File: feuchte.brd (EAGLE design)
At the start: 100 x 80 mm, 17 parts, among them IC1 ULN2003AD, IC2 IP4234CZ6, K1 G5LA, Q1 12MHz, U1 ATMEGA32U2-AU

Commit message: Bibliothek hinzugefügt
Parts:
- C1, C4, C5, C6, C7, R1, R2, R3: device eigene:0603 -> Bauelemente:0603
- C2, C3: device resistor:C0603K -> Bauelemente:0603
- IC2: value IP4234CZ6 -> ESD_USB_IP4234CZ6; device eigene:USB-ESD-IP4234CZ6 -> Bauelemente:USB_ESD_IP4234CZ6
- K1: value G5LA -> RELAY_G5LA; device eigene:G5LA -> Bauelemente:RELAY_G5LA
- Q1: device eigene:QUARZ-ABMM2 -> Bauelemente:QUARTZ_ABMM2
- U$1: value CON-SPI-10 -> CON_SPI_AVR10; device eigene:AVR-ISP-10 -> Bauelemente:CON_ISP_AVR10
- U1: value ATMEGA32U2-AU -> MCU_ATMEGA32U2-AU; device eigene:QFP80P900X900X120-32N -> Bauelemente:TQFP32-0.8
- USB1: value CON-MICROUSB-ZX62R-B-5P -> CON_MICROUSB_ZX62R-B-5P; device eigene:CON-MICROUSB_ZX62R-B-5P -> Bauelemente:CON_MICROUSB_ZX62R-B-5P
- moved C7 71.9 mm to (11.4, 37.9)
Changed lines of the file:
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@@
 </autorouter>
 <elements>
-<element name="U1" library="eigene" package="QFP80P900X900X120-32N" value="ATMEGA32U2-AU" x="40" y="20" rot="R90">
+<element name="U1" library="Bauelemente" package="TQFP32-0.8" value="MCU_ATMEGA32U2-AU" x="40" y="20" rot="R90">
 <attribute name="PACKAGE" value="TQFP-32" x="48.89" y="45.4" size="1.778" layer="27" rot="R90" display="off"/>
 <attribute name="OC_NEWARK" value="26R5632" x="48.89" y="45.4" size="1.778" layer="27" rot="R90" display="off"/>
@@
 <attribute name="OC_FARNELL" value="1748524" x="48.89" y="45.4" size="1.778" layer="27" rot="R90" display="off"/>
 </element>
-<element name="K1" library="eigene" package="G5LA" value="G5LA" x="-34.29" y="26.67"/>
+<element name="K1" library="Bauelemente" package="RELAY_G5LA" value="RELAY_G5LA" x="-34.29" y="26.67"/>
 <element name="IC1" library="uln-udn" package="SO16" value="ULN2003AD" x="-20.32" y="48.26"/>
-<element name="R1" library="eigene" package="0603" value="1k" x="-30.48" y="46.99"/>
-<element name="C1" library="eigene" package="0603" value="100n" x="9" y="17" rot="R270"/>
-<element name="Q1" library="eigene" package="QUARZ-ABMM2" value="12MHz" x="36" y="9"/>
-<element name="C2" library="resistor" package="C0603K" value="33p" x="36" y="5"/>
-<element name="C3" library="resistor" package="C0603K" value="33p" x="42" y="9" rot="R270"/>
-<element name="C4" library="eigene" package="0603" value="100n" x="30" y="16" rot="R270"/>
-<element name="C5" library="eigene" package="0603" value="1µ" x="30" y="21.55"/>
-<element name="C6" library="eigene" package="0603" value="10µ" x="21" y="16" rot="R270"/>
-<element name="R2" library="eigene" package="0603" value="22" x="25" y="19.95"/>
-<element name="R3" library="eigene" package="0603" value="22" x="25" y="18.45"/>
-<element name="USB1" library="eigene" package="CON-MICROUSB_ZX62R-B-5P" value="CON-MICROUSB-ZX62R-B-5P" x="4.8" y="19.525" rot="R270"/>
-<element name="IC2" library="eigene" package="USB-ESD-IP4234CZ6" value="IP4234CZ6" x="15" y="19.2" rot="R180"/>
-<element name="U$1" library="eigene" package="AVR-ISP-10" value="CON-SPI-10" x="43.4" y="29.8" rot="R180"/>
-<element name="C7" library="eigene" package="0603" value="100n" x="-37.9" y="-14.4"/>
+<element name="R1" library="Bauelemente" package="0603" value="1k" x="-30.48" y="46.99"/>
+<element name="C1" library="Bauelemente" package="0603" value="100n" x="9" y="17" rot="R270"/>
+<element name="Q1" library="Bauelemente" package="QUARTZ_ABMM2" value="12MHz" x="36" y="9"/>
+<element name="C2" library="Bauelemente" package="0603" value="33p" x="36" y="5"/>
+<element name="C3" library="Bauelemente" package="0603" value="33p" x="42" y="9" rot="R270"/>
+<element name="C4" library="Bauelemente" package="0603" value="100n" x="30" y="16" rot="R270"/>
+<element name="C5" library="Bauelemente" package="0603" value="1µ" x="30" y="21.55"/>
+<element name="C6" library="Bauelemente" package="0603" value="10µ" x="21" y="16" rot="R270"/>
+<element name="R2" library="Bauelemente" package="0603" value="22" x="25" y="19.95"/>
+<element name="R3" library="Bauelemente" package="0603" value="22" x="25" y="18.45"/>
+<element name="USB1" library="Bauelemente" package="CON_MICROUSB_ZX62R-B-5P" value="CON_MICROUSB_ZX62R-B-5P" x="4.8" y="19.525" rot="R270"/>
+<element name="IC2" library="Bauelemente" package="USB_ESD_IP4234CZ6" value="ESD_USB_IP4234CZ6" x="15" y="19.2" rot="R180"/>
+<element name="U$1" library="Bauelemente" package="CON_ISP_AVR10" value="CON_SPI_AVR10" x="43.4" y="29.8" rot="R180"/>
+<element name="C7" library="Bauelemente" package="0603" value="100n" x="11.4" y="37.9"/>
 </elements>
 <signals>
@@
 <contactref element="Q1" pad="4"/>
 <contactref element="Q1" pad="2"/>
-<wire x1="36.875" y1="5" x2="37.9" y2="5" width="0.5" layer="1"/>
+<wire x1="36.85" y1="5" x2="37.9" y2="5" width="0.5" layer="1"/>
 <wire x1="37.9" y1="5" x2="38.2" y2="5.3" width="0.5" layer="1" curve="90"/>
 <wire x1="38.2" y1="5.3" x2="38.2" y2="7.8" width="0.5" layer="1"/>
-<wire x1="42" y1="8.125" x2="38.5" y2="8.125" width="0.5" layer="1"/>
+<wire x1="42" y1="8.15" x2="38.5" y2="8.125" width="0.5" layer="1"/>
 <wire x1="38.5" y1="8.125" x2="38.2" y2="7.825" width="0.5" layer="1" curve="90"/>
 <wire x1="38.2" y1="7.825" x2="38.2" y2="7.8" width="0.5" layer="1"/>
@@
 <contactref element="C2" pad="1"/>
 <contactref element="U1" pad="1"/>
-<wire x1="35.125" y1="5" x2="34.1" y2="5" width="0.5" layer="1"/>
+<wire x1="35.15" y1="5" x2="34.1" y2="5" width="0.5" layer="1"/>
 <wire x1="34.1" y1="5" x2="33.8" y2="5.3" width="0.5" layer="1" curve="-90"/>
 <wire x1="33.8" y1="5.3" x2="33.8" y2="7.8" width="0.5" layer="1"/>
@@
 <contactref element="C3" pad="1"/>
 <contactref element="U1" pad="2"/>
-<wire x1="42" y1="9.875" x2="38.5" y2="9.875" width="0.5" layer="1"/>
+<wire x1="42" y1="9.85" x2="38.5" y2="9.875" width="0.5" layer="1"/>
 <wire x1="38.5" y1="9.875" x2="38.2" y2="10.175" width="0.5" layer="1" curve="-90"/>
 <wire x1="38.2" y1="10.175" x2="38.2" y2="10.2" width="0.5" layer="1"/>

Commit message: SMD Bauteile auf Rückseite gespiegelt
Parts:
- moved R1 126.1 mm to (95.2, 57.3), flipped to the bottom
- moved IC1 113.2 mm to (91.7, 64.4), flipped to the bottom
- moved USB1 90.4 mm to (95.2, 19.5), flipped to the bottom
- moved C1 82.0 mm to (91.0, 17.0), flipped to the bottom
- moved C7 81.0 mm to (90.4, 56.0), flipped to the bottom
- moved IC2 70.0 mm to (85.0, 19.2), flipped to the bottom
- moved C6 58.0 mm to (79.0, 16.0), flipped to the bottom
- moved U$1 55.9 mm to (77.8, 73.8)
- moved R2 50.0 mm to (75.0, 19.9), flipped to the bottom
- moved R3 50.0 mm to (75.0, 18.4), flipped to the bottom
- moved C4 40.0 mm to (70.0, 16.0), flipped to the bottom
- moved C5 40.0 mm to (70.0, 21.6), flipped to the bottom
- moved C2 28.0 mm to (64.0, 5.00), flipped to the bottom
- moved Q1 28.0 mm to (64.0, 9.00), flipped to the bottom
- moved U1 20.0 mm to (60.0, 20.0), flipped to the bottom
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
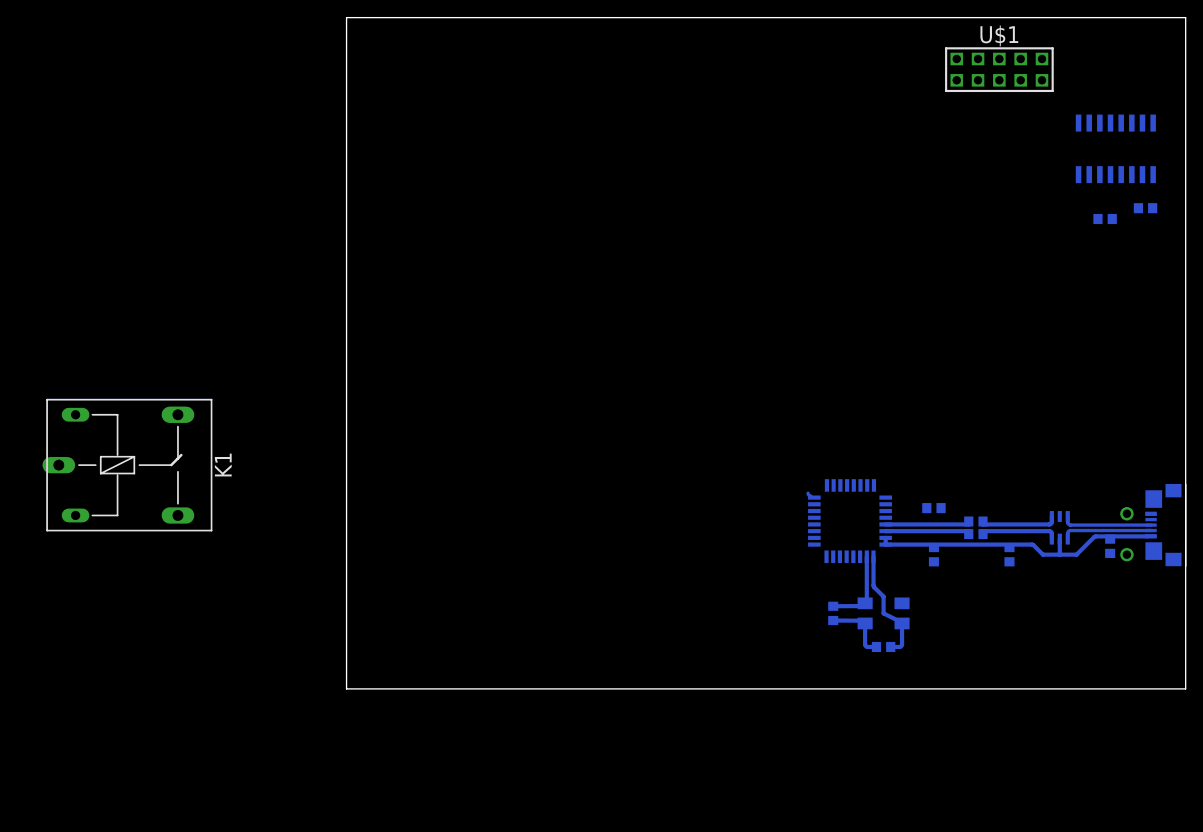
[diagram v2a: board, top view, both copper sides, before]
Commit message: ULN2003 aus Eagle verändert um fehler vom DRC zu entfernen und besser dem Datenblatt zu entsprechen
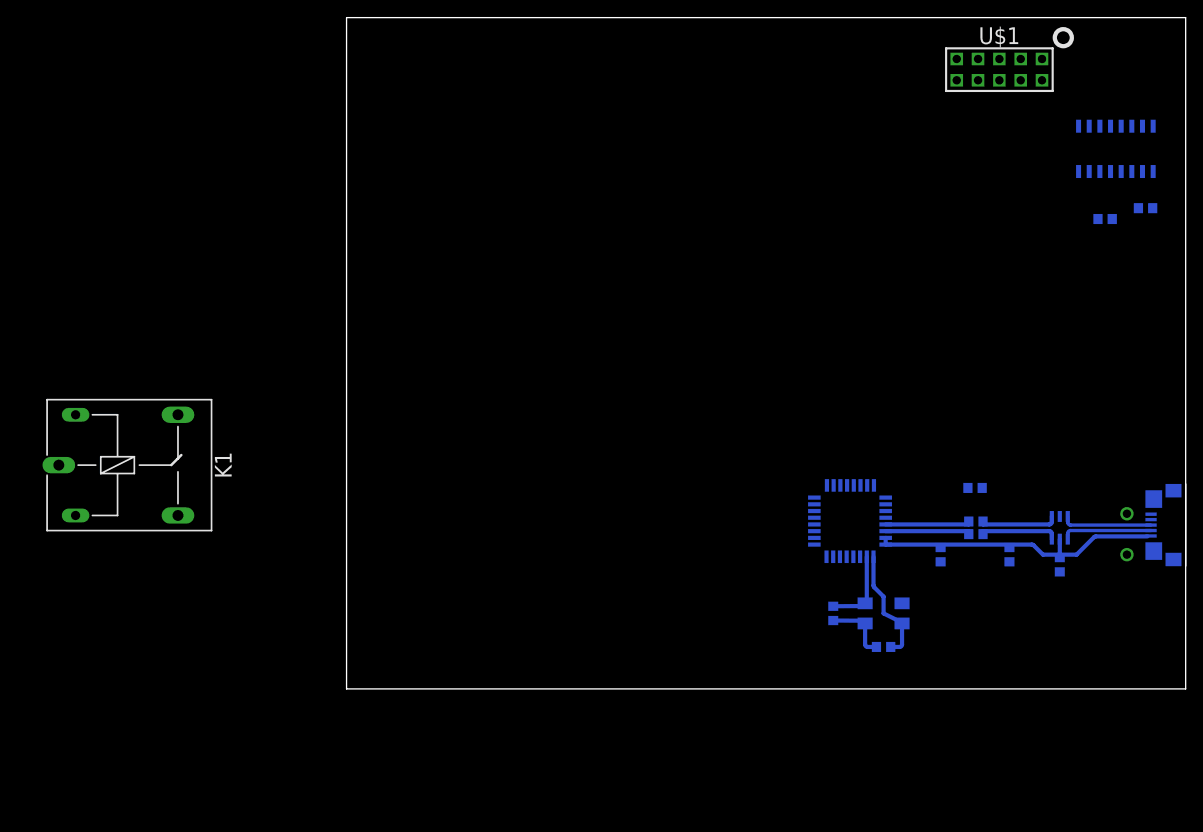
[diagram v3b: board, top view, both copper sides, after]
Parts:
- IC1: value ULN2003AD -> IC_ULN2003AD; device uln-udn:SO16 -> Bauelemente:SOIC16
- moved C1 6.39 mm to (85.0, 14.8)
- moved C5 5.46 mm to (74.9, 23.9)
- moved C4 0.80 mm to (70.8, 16.0)
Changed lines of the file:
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@@
 <layer number="24" name="bOrigins" color="15" fill="1" visible="yes" active="yes"/>
 <layer number="25" name="tNames" color="7" fill="1" visible="yes" active="yes"/>
-<layer number="26" name="bNames" color="7" fill="1" visible="yes" active="yes"/>
+<layer number="26" name="bNames" color="7" fill="1" visible="no" active="yes"/>
 <layer number="27" name="tValues" color="7" fill="1" visible="yes" active="yes"/>
-<layer number="28" name="bValues" color="7" fill="1" visible="yes" active="yes"/>
+<layer number="28" name="bValues" color="7" fill="1" visible="no" active="yes"/>
 <layer number="29" name="tStop" color="7" fill="3" visible="yes" active="yes"/>
 <layer number="30" name="bStop" color="7" fill="6" visible="yes" active="yes"/>
@@
 <wire x1="100" y1="80" x2="0" y2="80" width="0" layer="20"/>
 <wire x1="0" y1="80" x2="0" y2="0" width="0" layer="20"/>
-<rectangle x1="95.2" y1="17.925" x2="96.55" y2="18.425" layer="16" rot="R180"/>
-<rectangle x1="95.2" y1="20.625" x2="96.55" y2="21.125" layer="16" rot="R180"/>
 </plain>
 <attributes>
@@
 </element>
 <element name="K1" library="Bauelemente" package="RELAY_G5LA" value="RELAY_G5LA" x="-34.29" y="26.67"/>
-<element name="IC1" library="uln-udn" package="SO16" value="ULN2003AD" x="91.68" y="64.36" rot="MR0"/>
+<element name="IC1" library="Bauelemente" package="SOIC16" value="IC_ULN2003AD" x="91.68" y="64.36" rot="MR0"/>
 <element name="R1" library="Bauelemente" package="0603" value="1k" x="95.22" y="57.29" rot="MR0"/>
-<element name="C1" library="Bauelemente" package="0603" value="100n" x="91" y="17" rot="MR270"/>
+<element name="C1" library="Bauelemente" package="0603" value="100n" x="85" y="14.8" rot="MR270"/>
 <element name="Q1" library="Bauelemente" package="QUARTZ_ABMM2" value="12MHz" x="64" y="9" rot="MR0"/>
 <element name="C2" library="Bauelemente" package="0603" value="33p" x="64" y="5" rot="MR0"/>
 <element name="C3" library="Bauelemente" package="0603" value="33p" x="58" y="9" rot="MR270"/>
-<element name="C4" library="Bauelemente" package="0603" value="100n" x="70" y="16" rot="MR270"/>
-<element name="C5" library="Bauelemente" package="0603" value="1µ" x="70" y="21.55" rot="MR0"/>
+<element name="C4" library="Bauelemente" package="0603" value="100n" x="70.8" y="16" rot="MR270"/>
+<element name="C5" library="Bauelemente" package="0603" value="1µ" x="74.9" y="23.95" rot="MR0"/>
 <element name="C6" library="Bauelemente" package="0603" value="10µ" x="79" y="16" rot="MR270"/>
 <element name="R2" library="Bauelemente" package="0603" value="22" x="75" y="19.95" rot="MR0"/>
@@
 <signals>
 <signal name="GND" airwireshidden="yes">
-<contactref element="IC1" pad="8"/>
 <contactref element="USB1" pad="5"/>
 <contactref element="IC2" pad="2"/>
@@
 <contactref element="U$1" pad="6"/>
 <contactref element="U$1" pad="4"/>
+<contactref element="IC1" pad="8"/>
 <wire x1="77.8" y1="72.53" x2="80.34" y2="72.53" width="0" layer="19" extent="1-1"/>
 <wire x1="75.26" y1="72.53" x2="77.8" y2="72.53" width="0" layer="19" extent="1-1"/>
 <wire x1="72.72" y1="72.53" x2="75.26" y2="72.53" width="0" layer="19" extent="1-1"/>
-<wire x1="55.75" y1="20.4" x2="77.8" y2="72.53" width="0" layer="19" extent="1-1"/>
-<wire x1="61.2" y1="15.75" x2="55.75" y2="20.4" width="0" layer="19" extent="1-1"/>
-<wire x1="64.25" y1="20.4" x2="61.2" y2="15.75" width="0" layer="19" extent="1-1"/>
-<wire x1="70.85" y1="21.55" x2="64.25" y2="20.4" width="0" layer="19" extent="1-1"/>
-<wire x1="70" y1="15.15" x2="70.85" y2="21.55" width="0" layer="19" extent="1-1"/>
-<wire x1="66.2" y1="10.2" x2="70" y2="15.15" width="0" layer="19" extent="1-1"/>
-<wire x1="61.8" y1="7.825" x2="66.2" y2="10.2" width="0" layer="19" extent="1-1"/>
-<wire x1="79" y1="15.15" x2="70" y2="15.15" width="0" layer="19" extent="1-1"/>
-<wire x1="85" y1="20.55" x2="79" y2="15.15" width="0" layer="19" extent="1-1"/>
-<wire x1="91" y1="16.15" x2="85" y2="20.55" width="0" layer="19" extent="1-1"/>
-<wire x1="93" y1="16" x2="91" y2="16.15" width="0" layer="19" extent="1-1"/>
-<wire x1="93" y1="20.875" x2="93" y2="16" width="0" layer="19" extent="1-1"/>
-<wire x1="95.875" y1="20.825" x2="93" y2="20.875" width="0" layer="19" extent="1-1"/>
-<wire x1="87.235" y1="61.2866" x2="95.875" y2="20.875" width="0" layer="19" extent="1-1"/>
+<wire x1="87.235" y1="61.66" x2="80.34" y2="72.53" width="0" layer="19" extent="16-16"/>
+<wire x1="75.75" y1="23.95" x2="87.235" y2="61.66" width="0" layer="19" extent="16-16"/>
+<wire x1="79" y1="15.15" x2="75.75" y2="23.95" width="0" layer="19" extent="16-16"/>
+<wire x1="85" y1="13.95" x2="79" y2="15.15" width="0" layer="19" extent="16-16"/>
+<wire x1="85" y1="20.55" x2="85" y2="13.95" width="0" layer="19" extent="16-16"/>
+<wire x1="93" y1="20.875" x2="85" y2="20.55" width="0" layer="19" extent="16-16"/>
+<wire x1="95.875" y1="20.825" x2="93" y2="20.875" width="0" layer="19" extent="16-16"/>
+<wire x1="93" y1="16" x2="93" y2="20.875" width="0" layer="19" extent="1-1"/>
+<wire x1="70.8" y1="15.15" x2="79" y2="15.15" width="0" layer="19" extent="16-16"/>
+<wire x1="66.2" y1="10.2" x2="70.8" y2="15.15" width="0" layer="19" extent="16-16"/>
+<wire x1="61.8" y1="7.8" x2="66.2" y2="10.2" width="0" layer="19" extent="16-16"/>
+<wire x1="61.2" y1="15.75" x2="66.2" y2="10.2" width="0" layer="19" extent="16-16"/>
+<wire x1="64.25" y1="20.4" x2="61.2" y2="15.75" width="0" layer="19" extent="16-16"/>
+<wire x1="55.75" y1="20.4" x2="61.2" y2="15.75" width="0" layer="19" extent="16-16"/>
 </signal>
 <signal name="N$1">
@@
 <wire x1="85.95" y1="18.55" x2="86.275" y2="18.875" width="0.4" layer="16" curve="-90"/>
 <wire x1="86.275" y1="18.875" x2="95.875" y2="18.875" width="0.4" layer="16"/>
-<wire x1="85.95" y1="18.225" x2="85.95" y2="17.85" width="0" layer="19" extent="1-1"/>
+<wire x1="85.95" y1="18.225" x2="85.95" y2="17.85" width="0" layer="19" extent="16-16"/>
 </signal>
 <signal name="USBCON_P">
@@
 <contactref element="C4" pad="1"/>
 <contactref element="U$1" pad="2"/>
-<wire x1="60.4" y1="15.75" x2="82.88" y2="72.53" width="0" layer="19" extent="1-1"/>
-<wire x1="64.25" y1="17.2" x2="60.4" y2="15.75" width="0" layer="19" extent="1-1"/>
-<wire x1="91" y1="17.85" x2="89.299265625" y2="18.175" width="0" layer="19" extent="1-1"/>
-<wire x1="79" y1="16.85" x2="81.675734375" y2="17.2" width="0" layer="19" extent="1-1"/>
-<wire x1="70" y1="16.85" x2="64.25" y2="17.2" width="0" layer="19" extent="1-1"/>
+<wire x1="89.299265625" y1="18.175" x2="82.88" y2="72.53" width="0" layer="19" extent="16-16"/>
+<wire x1="85" y1="15.65" x2="85" y2="16" width="0" layer="19" extent="16-16"/>
+<wire x1="79" y1="16.85" x2="81.675734375" y2="17.2" width="0" layer="19" extent="16-16"/>
+<wire x1="60.4" y1="15.75" x2="64.25" y2="17.2" width="0" layer="19" extent="16-16"/>
+<wire x1="70.8" y1="16.85" x2="64.25" y2="17.2" width="0" layer="19" extent="16-16"/>
 </signal>
 <signal name="N$7">
-<wire x1="55" y1="23.325" x2="55.325" y2="23" width="0.4" layer="16" curve="90" cap="flat"/>
+<wire x1="55" y1="23.325" x2="55.325" y2="23" width="0" layer="19" curve="90" cap="flat" extent="1-16"/>
 </signal>
 <signal name="USBR_P">
@@
 <contactref element="U1" pad="27"/>
 <contactref element="C5" pad="2"/>
-<wire x1="69.15" y1="21.55" x2="64.25" y2="21.2" width="0" layer="19" extent="1-1"/>
+<wire x1="64.25" y1="21.2" x2="74.05" y2="23.95" width="0" layer="19" extent="16-16"/>
 </signal>
 <signal name="N$3">
 <contactref element="U$1" pad="7"/>
 <contactref element="U1" pad="15"/>
-<wire x1="55.75" y1="22" x2="75.26" y2="75.07" width="0" layer="19" extent="1-1"/>
+<wire x1="55.75" y1="22" x2="75.26" y2="75.07" width="0" layer="19" extent="16-16"/>
 </signal>
 <signal name="N$4">
 <contactref element="U$1" pad="1"/>
 <contactref element="U1" pad="16"/>
-<wire x1="55.75" y1="22.8" x2="82.88" y2="75.07" width="0" layer="19" extent="1-1"/>
+<wire x1="55.75" y1="22.8" x2="82.88" y2="75.07" width="0" layer="19" extent="16-16"/>
 </signal>
 <signal name="N$5">
 <contactref element="U$1" pad="9"/>
 <contactref element="U1" pad="17"/>
-<wire x1="57.25" y1="24.25" x2="72.72" y2="75.07" width="0" layer="19" extent="1-1"/>
+<wire x1="57.25" y1="24.25" x2="72.72" y2="75.07" width="0" layer="19" extent="16-16"/>
 </signal>
 <signal name="N$6">
 <contactref element="U1" pad="24"/>
 <contactref element="U$1" pad="5"/>
-<wire x1="62.85" y1="24.25" x2="77.8" y2="75.07" width="0" layer="19" extent="1-1"/>
+<wire x1="62.85" y1="24.25" x2="77.8" y2="75.07" width="0" layer="19" extent="16-16"/>
 </signal>
 </signals>

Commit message: abends gehts nach hause
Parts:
- added C10, C8, C9: 100n, Bauelemente:0603
- added CON1, CON2: CON_PCB_7.5MM_3-POLE, Bauelemente:CON_PCB_7.5MM_3-POLE
- added K2: RELAY_G5LA, Bauelemente:RELAY_G5LA
- moved USB1 76.1 mm to (41.5, 73.4), turned to 180 degrees
- moved R1 68.2 mm to (41.8, 14.8)
- moved K1 67.8 mm to (29.7, 49.0), turned to 180 degrees
- moved C1 65.0 mm to (46.2, 66.9), turned to 180 degrees
- moved IC2 64.4 mm to (41.8, 66.9), turned to 90 degrees
- moved IC1 59.3 mm to (32.6, 59.5), turned to 270 degrees
- moved U$1 58.6 mm to (34.0, 34.8)
- moved C6 56.3 mm to (53.8, 66.3), turned to 180 degrees
- moved R3 52.3 mm to (42.5, 59.5), turned to 270 degrees
- moved R2 52.1 mm to (41.0, 59.5), turned to 270 degrees
- moved C7 50.8 mm to (43.7, 35.9)
- moved C4 49.8 mm to (53.9, 62.8), turned to 180 degrees
- moved C2 48.8 mm to (56.0, 53.1), turned to 270 degrees
- moved Q1 45.7 mm to (52.0, 53.1), turned to 270 degrees
- moved C5 41.6 mm to (35.4, 10.9), turned to 180 degrees
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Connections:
- net N$12 renamed +3V3
- new net CAP: R1.2
- new net N$10: C10.1, C9.2
- new net N$11: IC1.2, U1.23
- new net N$12: IC1.7, U1.21
- new net N$13: IC1.10, K1.1
- new net N$14: IC1.15, K2.2
- new net N$15: CON1.1, K1.S
- new net N$16: CON1.3, K1.O
- new net N$17: CON2.1, K2.S
- new net N$18: CON2.2, K2.P
- new net N$19: CON2.3, K2.O
- new net N$7: CON1.2, K1.P
- new net N$8: C7.1, C8.1, C9.1, U1.7
- new net N$9: C10.2, C7.2, C8.2, R1.1, U1.8
- net +5V: now also IC1.9, K1.2, K2.1
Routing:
- net N$7: track 0.00 -> 24.8 mm
- net N$18: track 0.00 -> 24.8 mm
- net N$19: track 0.00 -> 12.1 mm
- net N$17: track 0.00 -> 12.1 mm
- net N$16: track 0.00 -> 12.1 mm
- net N$15: track 0.00 -> 12.1 mm
- net USBC_N: track 10.3 -> 5.65 mm
- net USBC_P: track 10.3 -> 5.65 mm
- net +5V: track 35.6 -> 39.9 mm
- net USBCON_P: track 10.8 -> 7.06 mm
- net USBCON_N: track 10.4 -> 6.68 mm
- net N$14: track 0.00 -> 2.75 mm
- net N$13: track 0.00 -> 2.75 mm
- net USBR_N: track 9.32 -> 6.72 mm
- net USBR_P: track 9.32 -> 6.72 mm
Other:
- outline, holes or cut-outs redrawn

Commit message: Weiter gelayouted
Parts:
- moved C4 23.2 mm to (77.1, 62.1)
- moved C6 21.3 mm to (75.1, 67.5)
- moved CON1 21.0 mm to (4.95, 70.0)
- moved CON2 21.0 mm to (4.95, 49.0)
- moved K1 21.0 mm to (29.7, 70.0)
- moved K2 21.0 mm to (29.7, 49.0)
- moved C1 5.76 mm to (44.4, 72.3)
- moved USB1 4.36 mm to (37.5, 75.2)
- moved IC2 4.28 mm to (38.9, 70.0)
- moved R2 1.80 mm to (41.0, 61.3)
- moved R3 1.80 mm to (42.5, 61.3)
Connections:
- net USBCON_P renamed USBCON_
- net +5V: now also K1.1, K2.2; no longer K1.2, K2.1
- net N$11: now also IC1.7; no longer IC1.2
- net N$12: now also IC1.2; no longer IC1.7
- net N$13: now also K2.1; no longer K1.1
- net N$14: now also K1.2; no longer K2.2
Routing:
- net +5V: track 39.9 -> 56.9 mm
- net N$12: track 0.00 -> 9.50 mm
- net GND: track 7.97 -> 17.0 mm
- net USBR_P: track 6.72 -> 0.00 mm
- net USBR_N: track 6.72 -> 0.00 mm
- net USBC_P: track 5.65 -> 0.35 mm
- net USBC_N: track 5.65 -> 0.35 mm
- net N$1: track 13.7 -> 9.75 mm
- net N$2: track 9.58 -> 6.08 mm
- net N$11: track 0.00 -> 2.20 mm
- net USBCON_: track 7.06 -> 6.06 mm
- net USBCON_N: track 6.68 -> 5.92 mm
